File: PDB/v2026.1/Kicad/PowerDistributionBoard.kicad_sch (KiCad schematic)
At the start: 56 parts, among them J1 12V_EXP3, J10 24V_IN, J12 Suspension_Linear_Pot1, J13 Suspension_Linear_Pot2, J14 Suspension_Linear_Pot3, J15 Suspension_Linear_Pot4, J16 CCM_Faults, J17 EXP1_5V, J18 RasPI_5V, J19 LATCH_12V, J2 12V_EXP2, J20 Throttle_Sensor, J24 Wheel_Sensor1, J25 Wheel_Sensor2, J26 3V3_EXP, J27 BATTERY_12V, J28 BATTERY_GND, J29 BATTERY_24V, J3 12V_EXP1, J35 24V_EXP1, J4 RTM, J5 CCM_12V, J6 Back_Of_Car_12V, J7 BSPD, J8 LATCH, J9 24V_OUT, U1 5to3.3_Linear_Regulator, U2 TLV76150DCYR

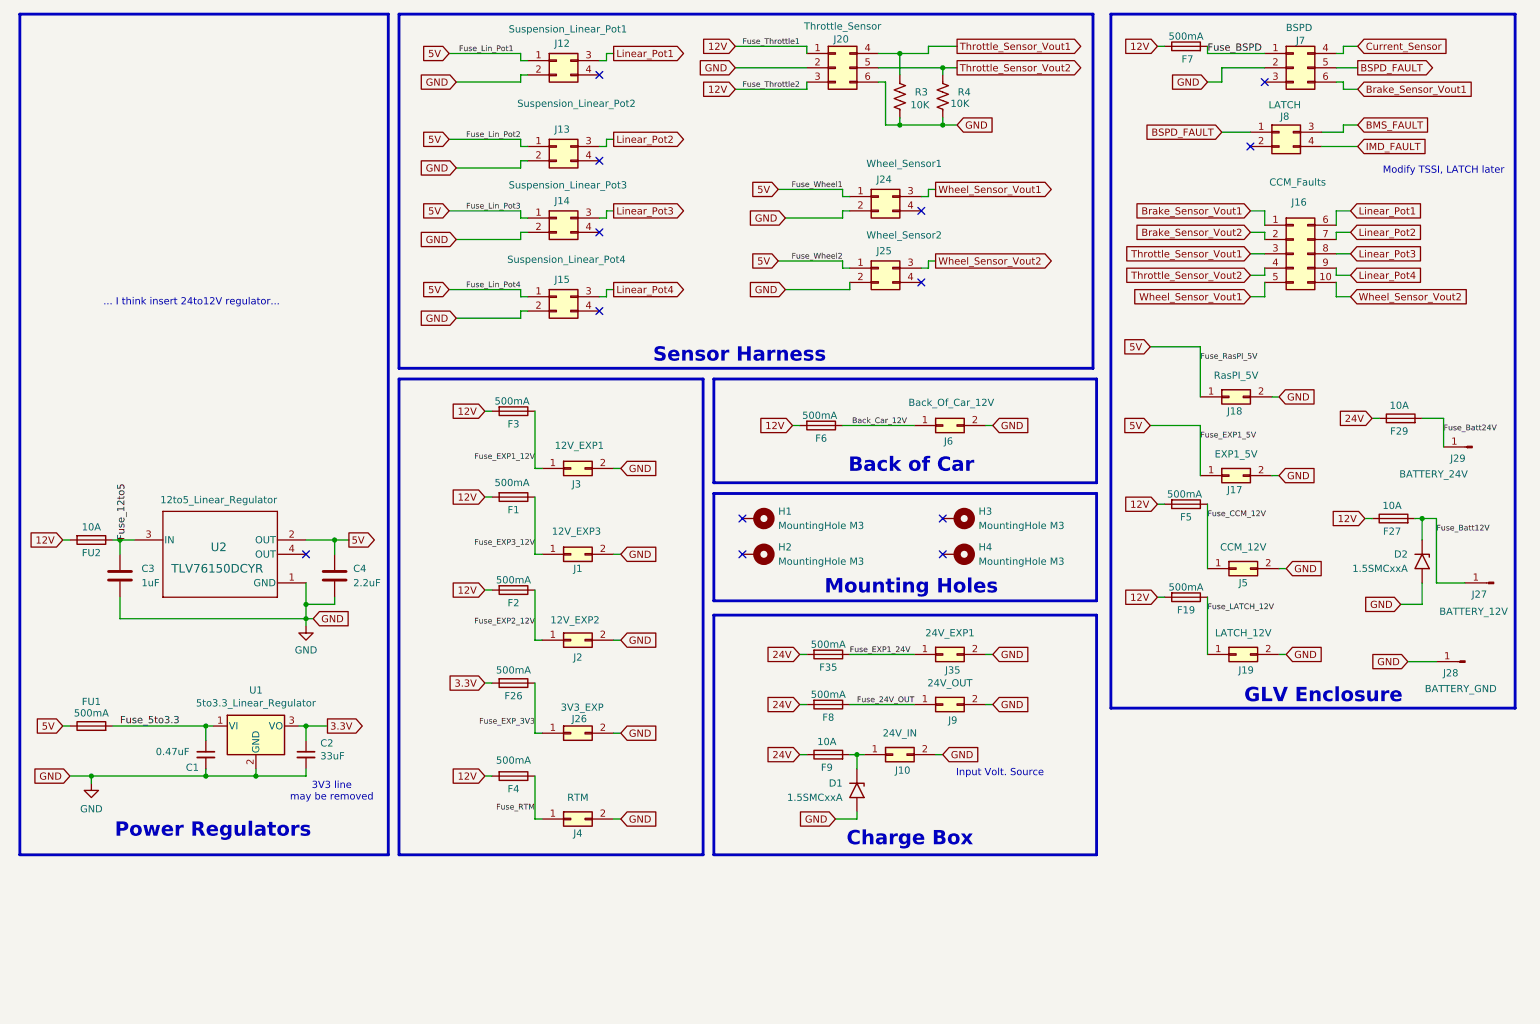
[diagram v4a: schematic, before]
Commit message: Reduced PDB size, power planes just started
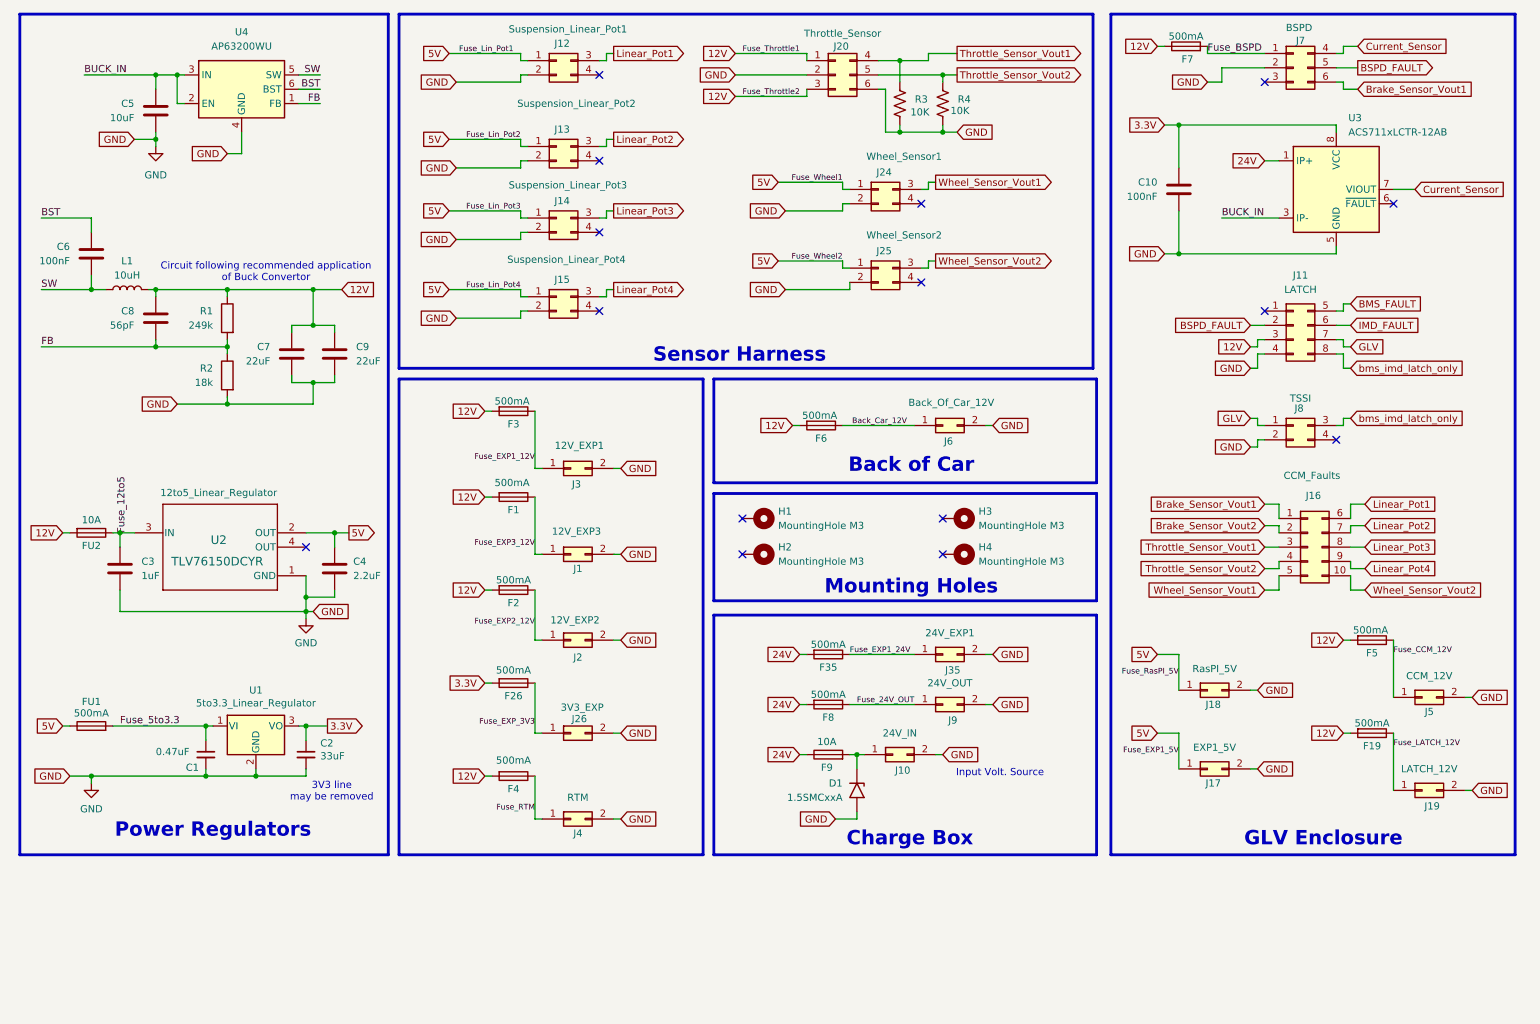
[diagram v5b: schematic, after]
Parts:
- removed D2: 1.5SMCxxA, Diode_SMD:D_SMC, symbol Diode:1.5SMCxxA
- removed F27, F29: 10A, 0footprints:FUSE_3522-2, symbol Device:Fuse
- removed J27: BATTERY_12V, 0footprints:KEYSTONE_7797, symbol Connector:Conn_01x01_Pin
- removed J28: BATTERY_GND, 0footprints:KEYSTONE_7797, symbol Connector:Conn_01x01_Pin
- removed J29: BATTERY_24V, 0footprints:KEYSTONE_7797, symbol Connector:Conn_01x01_Pin
- added C10, C6: 100nF, Capacitor_SMD:C_0603_1608Metric_Pad1.08x0.95mm_HandSolder, symbol Device:C
- added C5: 10uF, Capacitor_SMD:C_0603_1608Metric_Pad1.08x0.95mm_HandSolder, symbol Device:C
- added C7, C9: 22uF, Capacitor_SMD:C_0603_1608Metric_Pad1.08x0.95mm_HandSolder, symbol Device:C
- added C8: 56pF, Capacitor_SMD:C_0603_1608Metric_Pad1.08x0.95mm_HandSolder, symbol Device:C
- added J11: LATCH, 0footprints:Molex_Mini-Fit_Jr_5566-08A_2x04_P4.20mm_Vertical, symbol Connector_Generic:Conn_02x04_Top_Bottom
- added L1: 10uH, Inductor_SMD:L_0603_1608Metric_Pad1.05x0.95mm_HandSolder, symbol Device:L
- added R1: 249k, Resistor_SMD:R_0603_1608Metric_Pad0.98x0.95mm_HandSolder, symbol Device:R
- added R2: 18k, Resistor_SMD:R_0603_1608Metric_Pad0.98x0.95mm_HandSolder, symbol Device:R
- added U3: ACS711xLCTR-12AB, Package_SO:SOIC-8_3.9x4.9mm_P1.27mm, symbol Sensor_Current:ACS711xLCTR-12AB
- added U4: AP63200WU, Package_TO_SOT_SMD:TSOT-23-6, symbol Regulator_Switching:AP63200WU
- J8: value LATCH -> TSSI
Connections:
- net 12V: now also C7.1, C8.1, C9.1, J11.3 (Pin_3), L1.2, R1.1
- net 24V: now also U3.1 (IP+), U3.2 (IP+)
- net 3.3V: now also C10.2, U3.8 (VCC)
- net BMS_FAULT: now also J11.5 (Pin_5); no longer J8.3 (Pin_3)
- net BSPD_FAULT: now also J11.2 (Pin_2); no longer J8.1 (Pin_1)
- net Current_Sensor: now also U3.7 (VIOUT)
- net GND: now also J8.2 (Pin_2), C10.1, C5.2, C7.2, C9.2, J11.4 (Pin_4), R2.2, U3.5 (GND), U4.4 (GND)
- net IMD_FAULT: now also J11.6 (Pin_6); no longer J8.4 (Pin_4)
- new net BST: C6.2, U4.6 (BST)
- new net BUCK_IN: C5.1, U3.3 (IP-), U3.4 (IP-), U4.2 (EN), U4.3 (IN)
- new net FB: C8.2, R1.2, R2.1, U4.1 (FB)
- new net GLV: J11.7 (Pin_7), J8.1 (Pin_1)
- new net SW: C6.1, L1.1, U4.5 (SW)
- new net bms_imd_latch_only: J11.8 (Pin_8), J8.3 (Pin_3)
- no-connect marks 13 -> 15
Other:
- note added: "Circuit following recommended application of Buck Convertor"
- note removed: "... I think insert 24to12V regulator..."
- note removed: "Modify TSSI, LATCH later"
- moved on the sheet: C3, C4, F19, F5, FU2, J16, J17, J18, J19, J20, J24, J5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

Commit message: Changed a buncha stuff on other ppl's board. established new branch
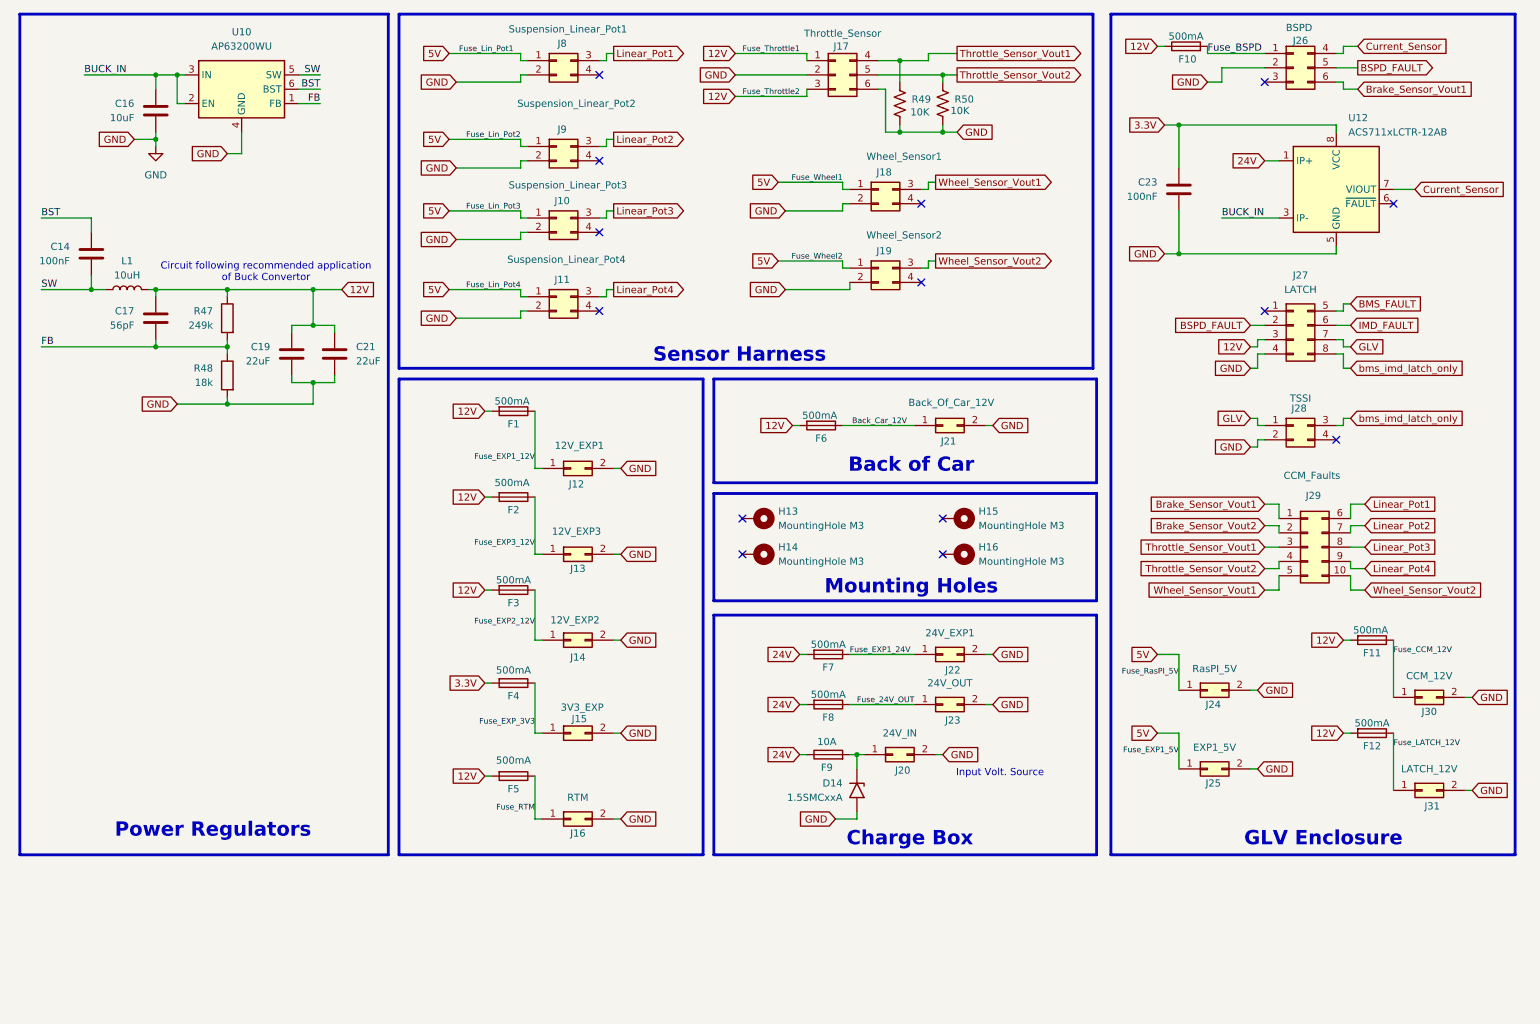
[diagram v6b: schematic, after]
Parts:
- removed C1: 0.47uF, Capacitor_SMD:C_0805_2012Metric, symbol Device:C_Small
- removed C2: 33uF, Capacitor_SMD:C_0805_2012Metric, symbol Device:C_Small
- removed C3: 1uF, Capacitor_SMD:C_0805_2012Metric, symbol Device:C
- removed C4: 2.2uF, Capacitor_SMD:C_0805_2012Metric, symbol Device:C
- removed FU1: 500mA, 0footprints:FUSE_3522-2, symbol Device:Fuse
- removed FU2: 10A, 0footprints:FUSE_3522-2, symbol Device:Fuse
- removed U1: 5to3.3_Linear_Regulator, Package_TO_SOT_THT:TO-220-3_Vertical, symbol Regulator_Linear:LF15_TO220
- removed U2: TLV76150DCYR, Package_TO_SOT_SMD:SOT-223, symbol 2025-04-04_22-39-47:TLV76150DCYR
- renumbered C6 to C14, C5 to C16, C8 to C17, C7 to C19, C9 to C21, C10 to C23, D1 to D14, F3 to F1, F7 to F10, F5 to F11, F19 to F12, F1 to F2, F2 to F3, F26 to F4, F4 to F5, F35 to F7, H1 to H13, H2 to H14, H3 to H15, H4 to H16, J14 to J10, J15 to J11, J3 to J12, J1 to J13, J2 to J14, J26 to J15, J4 to J16, J20 to J17, J24 to J18, J25 to J19, J10 to J20, J6 to J21, J35 to J22, J9 to J23, J18 to J24, J17 to J25, J7 to J26, J11 to J27, J8 to J28, J16 to J29, J5 to J30, J19 to J31, J12 to J8, J13 to J9, R1 to R47, R2 to R48, R3 to R49, R4 to R50, U4 to U10, U3 to U12
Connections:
- no-connect marks 15 -> 14
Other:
- note removed: "3V3 line may be removed"
